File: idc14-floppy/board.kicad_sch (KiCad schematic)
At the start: 18 parts, among them J1 61900411021, J3 2x7, J4 02x17, J5 629105150521, SW1 SW_DPDT_x2

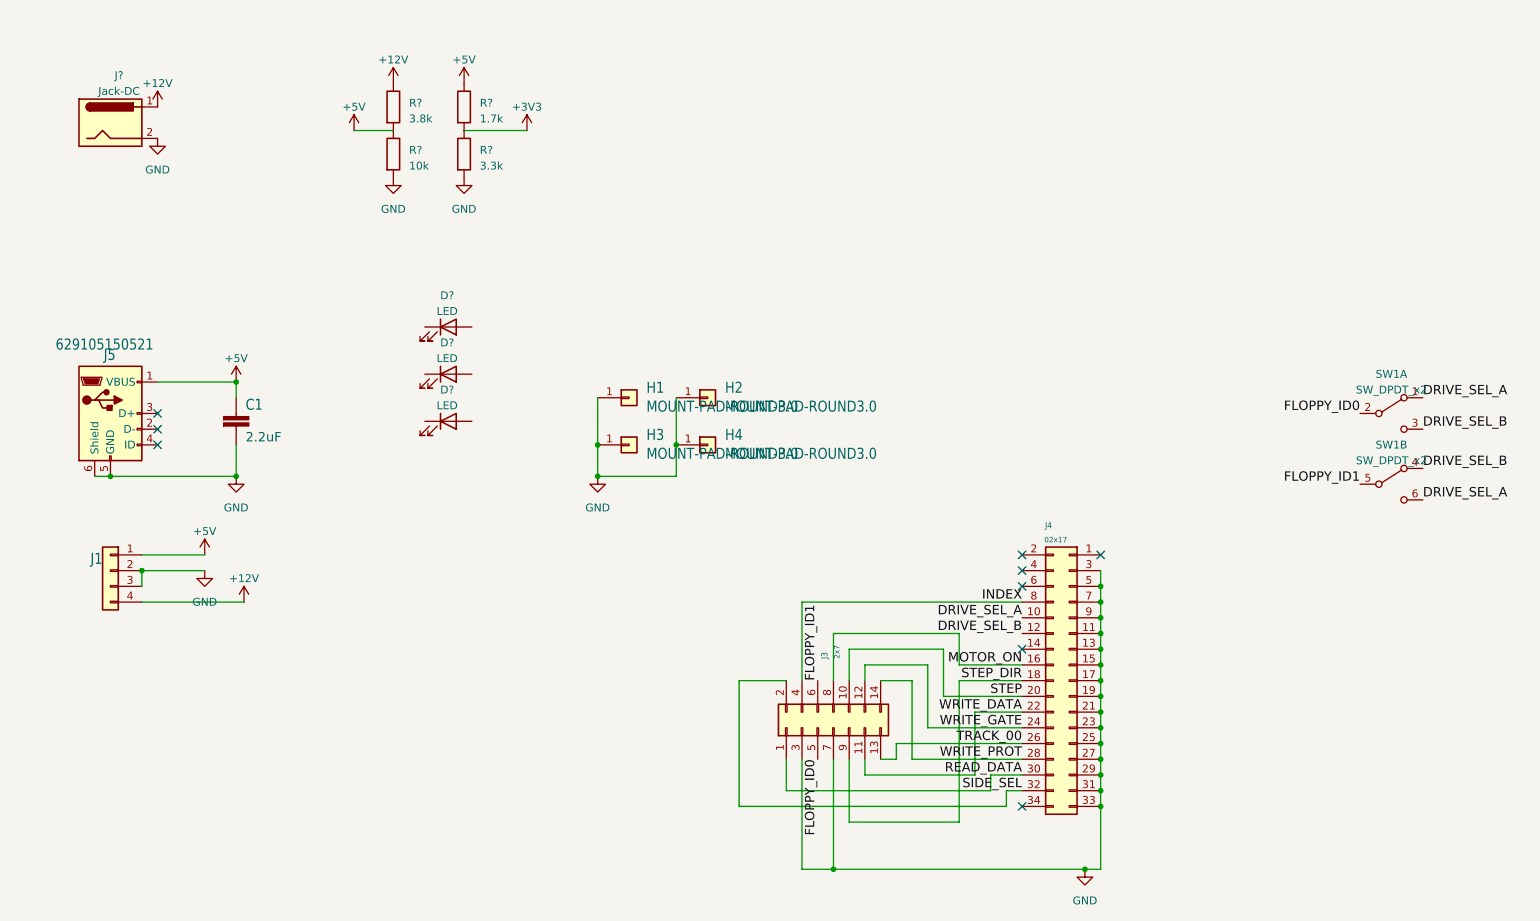
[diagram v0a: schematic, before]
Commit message: reorganize, start enclosure
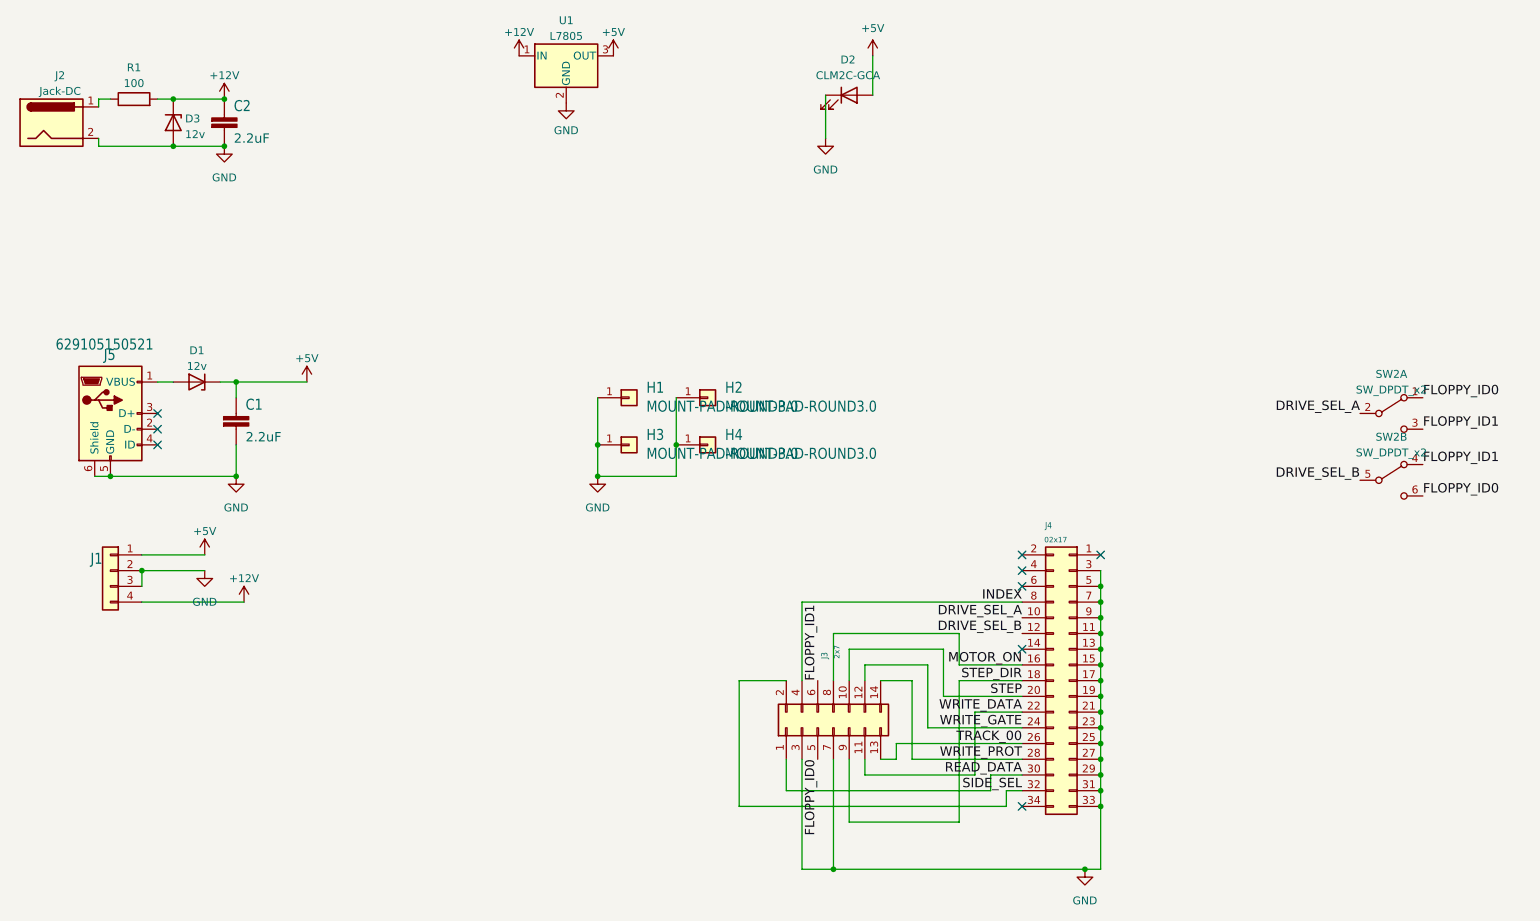
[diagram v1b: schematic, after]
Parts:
- removed D? (x3): LED, symbol Device:LED
- removed R?: 1.7k, symbol Device:R
- removed R?: 3.3k, symbol Device:R
- removed R?: 10k, symbol Device:R
- removed R?: 3.8k, symbol Device:R
- removed SW1: SW_DPDT_x2, Connector_PinHeader_2.54mm:PinHeader_2x03_P2.54mm_Vertical, symbol Switch:SW_DPDT_x2
- added C2: 2.2uF, Capacitor_SMD:C_0603_1608Metric, symbol board-eagle-import:C-EUC0805K
- added D1, D3: 12v, Diode_SMD:D_0603_1608Metric, symbol Device:D_Zener
- added D2: CLM2C-GCA, LED_SMD:LED_Cree-PLCC4_3.2x2.8mm_CCW, symbol Device:LED
- added R1: 100, Resistor_SMD:R_0603_1608Metric, symbol Device:R
- added SW2: SW_DPDT_x2, Button_Switch_THT:SW_E-Switch_EG2219_DPDT_Angled, symbol Switch:SW_DPDT_x2
- added U1: L7805, Package_TO_SOT_SMD:TO-263-2, symbol Regulator_Linear:L7805
- J1: value 61900411021 -> 171826-4
- J2: renamed from J?; footprint (none) -> Connector_BarrelJack:BarrelJack_Horizontal
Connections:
- net +12V: now also C2.1, D3.1 (K), R1.2, U1.1 (IN); no longer J2.1
- net +5V: now also D1.1 (K), D2.2 (A), U1.3 (OUT); no longer J5.1 (VBUS)
- net DRIVE_SEL_A: now also SW2.2 (B)
- net DRIVE_SEL_B: now also SW2.5 (B)
- net FLOPPY_ID0: now also SW2.1 (A), SW2.6 (C)
- net FLOPPY_ID1: now also SW2.3 (C), SW2.4 (A)
- net GND: now also C2.2, D2.4 (K), D3.2 (A), U1.2 (GND)
- new net: J2.1, R1.1
- new net: D1.2 (A), J5.1 (VBUS)
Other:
- moved on the sheet: J2

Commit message: footprint
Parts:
- removed D3: 12v, Diode_SMD:D_0603_1608Metric, symbol Device:D_Zener
- removed R1: 100, Resistor_SMD:R_0603_1608Metric, symbol Device:R
- added D3: D_TVS, symbol Device:D_TVS
- added R2: 10k, Resistor_SMD:R_0603_1608Metric, symbol Device:R
- added R3: 1.78k, Resistor_SMD:R_0603_1608Metric, symbol Device:R
- added R4: 3.16k, Resistor_SMD:R_0603_1608Metric, symbol Device:R
- D2: value CLM2C-GCA -> LED; footprint LED_SMD:LED_Cree-PLCC4_3.2x2.8mm_CCW -> LED_SMD:LED_0603_1608Metric
- J1: footprint Connector_PinHeader_2.54mm:PinHeader_1x04_P2.54mm_Vertical -> parts:171826-4
- J2: symbol Connector:Jack-DC -> Connector:Barrel_Jack_MountingPin
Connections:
- net +12V: now also J2.1
- net +5V: now also R3.1; no longer D2.2 (A)
- net GND: now also D2.1 (K), J2.MP (MountPin), SW2.MP, R4.2; no longer D2.4 (K)
- new net: D2.2 (A), R2.1
- new net: R2.2, R3.2, R4.1

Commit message: 1.10 final
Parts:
- removed C2: 2.2uF, Capacitor_SMD:C_0603_1608Metric, symbol board-eagle-import:C-EUC0805K
- removed D1: 12v, Diode_SMD:D_0603_1608Metric, symbol Device:D_Zener
- removed D3: D_TVS, symbol Device:D_TVS
- removed J2: Jack-DC, Connector_BarrelJack:BarrelJack_Horizontal, symbol Connector:Barrel_Jack_MountingPin
- removed U1: L7805, Package_TO_SOT_SMD:TO-263-2, symbol Regulator_Linear:L7805
- D2: value LED -> PWR
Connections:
- net +5V: now also J5.1 (VBUS)
- net GND: now also J4.1 (Pin_1); no longer C1.2
- net +3V3: now reaches R2.2, R3.2, R4.1
- net +12V: no longer names the net of J1.4 (Pin_4)
- new net VSS: C1.2
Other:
- moved on the sheet: C1, D2, J5, R2, R3, R4

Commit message: 1.2 test
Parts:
- removed J3: 2x7, Connector_IDC:IDC-Header_2x07_P2.54mm_Horizontal, symbol Connector_Generic:Conn_02x07_Odd_Even
- added J3: Conn_02x07, Connector_IDC:IDC-Header_2x07_P2.54mm_Horizontal, symbol Connector_Generic:Conn_01x14
- added JP1: SW_SPST, symbol Switch:SW_SPST
- added R5, R6, R7, R8, R9: 1k, Resistor_SMD:R_0805_2012Metric, symbol Device:R
- C1: footprint Capacitor_SMD:C_0603_1608Metric -> Capacitor_SMD:C_0805_2012Metric
- D2: footprint LED_SMD:LED_0603_1608Metric -> LED_SMD:LED_0805_2012Metric
- R2, R3, R4: footprint Resistor_SMD:R_0603_1608Metric -> Resistor_SMD:R_0805_2012Metric
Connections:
- net +5V: now also JP1.2 (B)
- net FLOPPY_ID0: now also J3.5 (Pin_5)
- net FLOPPY_ID1: now also J3.6 (Pin_6)
- net GND: now also J3.3 (Pin_3), J3.7 (Pin_7)
- net INDEX: now also J3.4 (Pin_4)
- net READ_DATA: now also J3.1 (Pin_1)
- net SIDE_SEL: now also J3.2 (Pin_2)
- net MOTOR_ON renamed ~{MOTOR_ON}
- net ~{MOTOR_ON}: now also J3.8 (Pin_8), R9.2
- net STEP renamed ~{STEP}
- net ~{STEP}: now also J3.10 (Pin_10), R8.2
- net STEP_DIR renamed ~{STEP_DIR}
- net ~{STEP_DIR}: now also J3.9 (Pin_9), R7.2
- net TRACK_00 renamed ~{TRACK_00}
- net ~{TRACK_00}: now also J3.13 (Pin_13)
- net WRITE_DATA renamed ~{WRITE_DATA}
- net ~{WRITE_DATA}: now also J3.11 (Pin_11), R5.2
- net WRITE_GATE renamed ~{WRITE_GATE}
- net ~{WRITE_GATE}: now also J3.12 (Pin_12), R6.2
- net WRITE_PROT renamed ~{WRITE_PROT}
- new net: JP1.1 (A), R5.1, R6.1, R7.1, R8.1, R9.1
- new net ~{WRITE_PROTECT}: J3.14 (Pin_14)
